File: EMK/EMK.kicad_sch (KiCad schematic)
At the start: 76 parts, among them J1 USB_C_Receptacle_USB2.0_14P, J2 Conn_01x02_Socket, J3 Conn_ARM_JTAG_SWD_10, Q1 Si2371EDS, SW1 SW_Nidec_CAS-120A1, SW10 MX9, SW11 MX13, SW12 MX10, SW13 MX14, SW14 MX11, SW15 MX15, SW16 MX12, SW17 MX16, SW2 MX1, SW3 MX2, SW4 MX3, SW5 MX4, SW6 MX5, SW7 MX6, SW8 MX7, SW9 MX8, U1 nRF52840-QFAA, U2 15nH, U3 TPS62822DLC, U4 USBLC6-2SC6, U5 TP4057, Y1 Crystal_32.768kHz, Y2 Crystal_32mHz

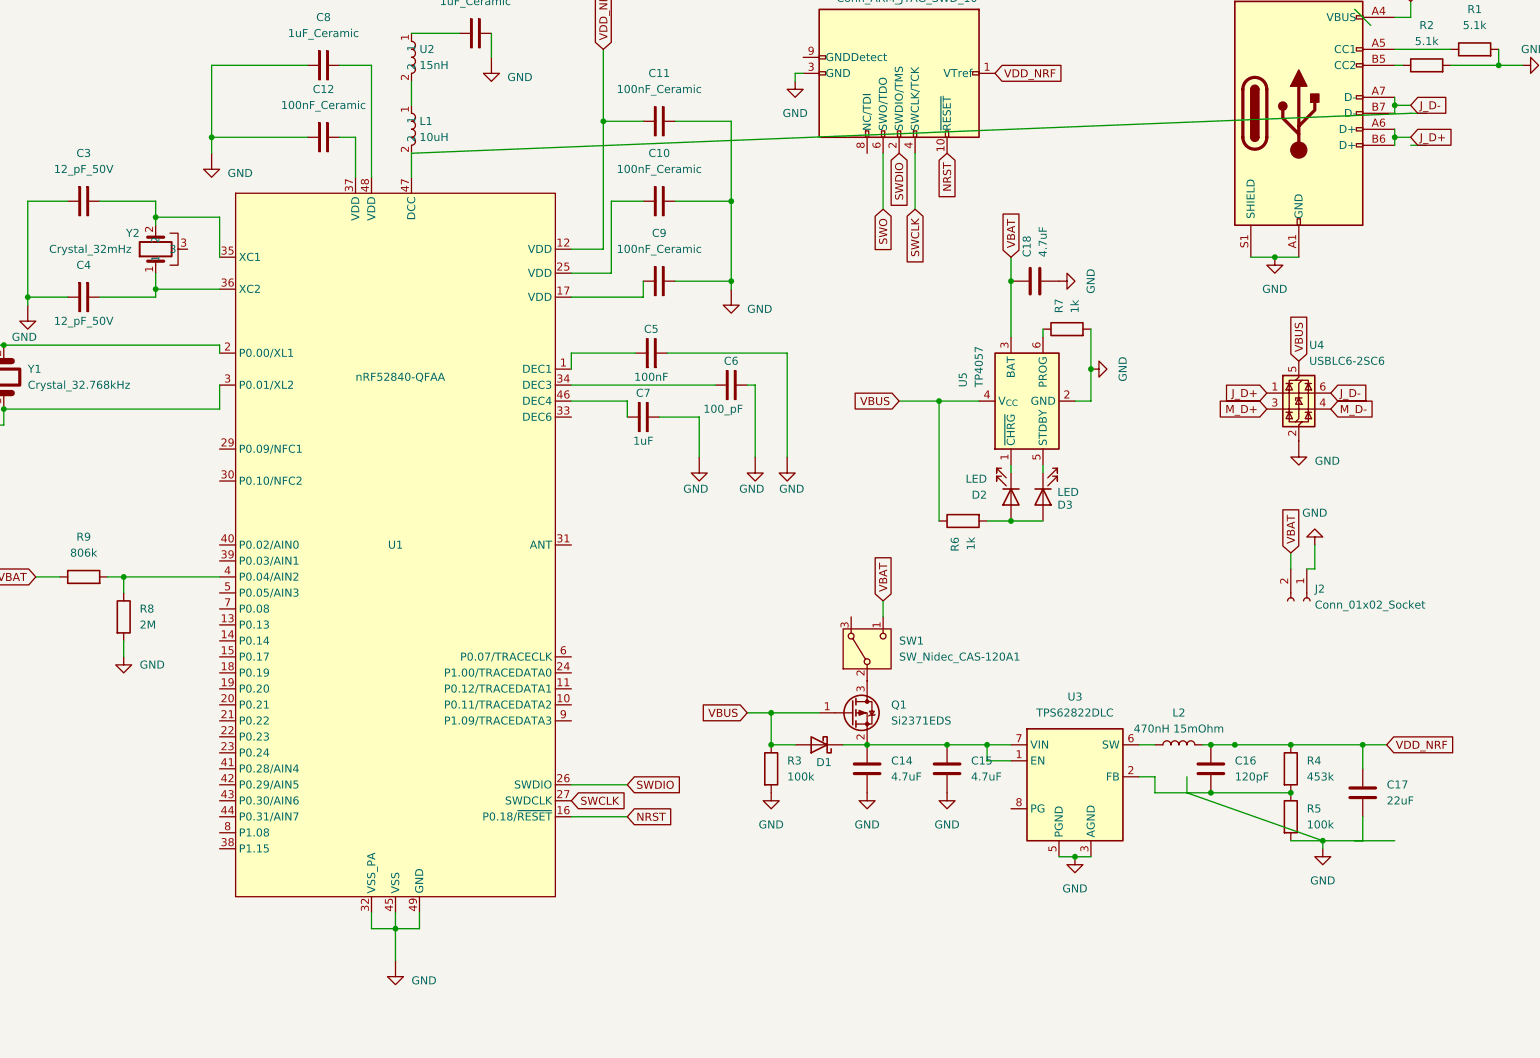
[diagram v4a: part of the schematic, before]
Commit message: feat: adiciona o conector SWD.
Signed-off-by: Paulo Santos <prms@ic.ufal.br>
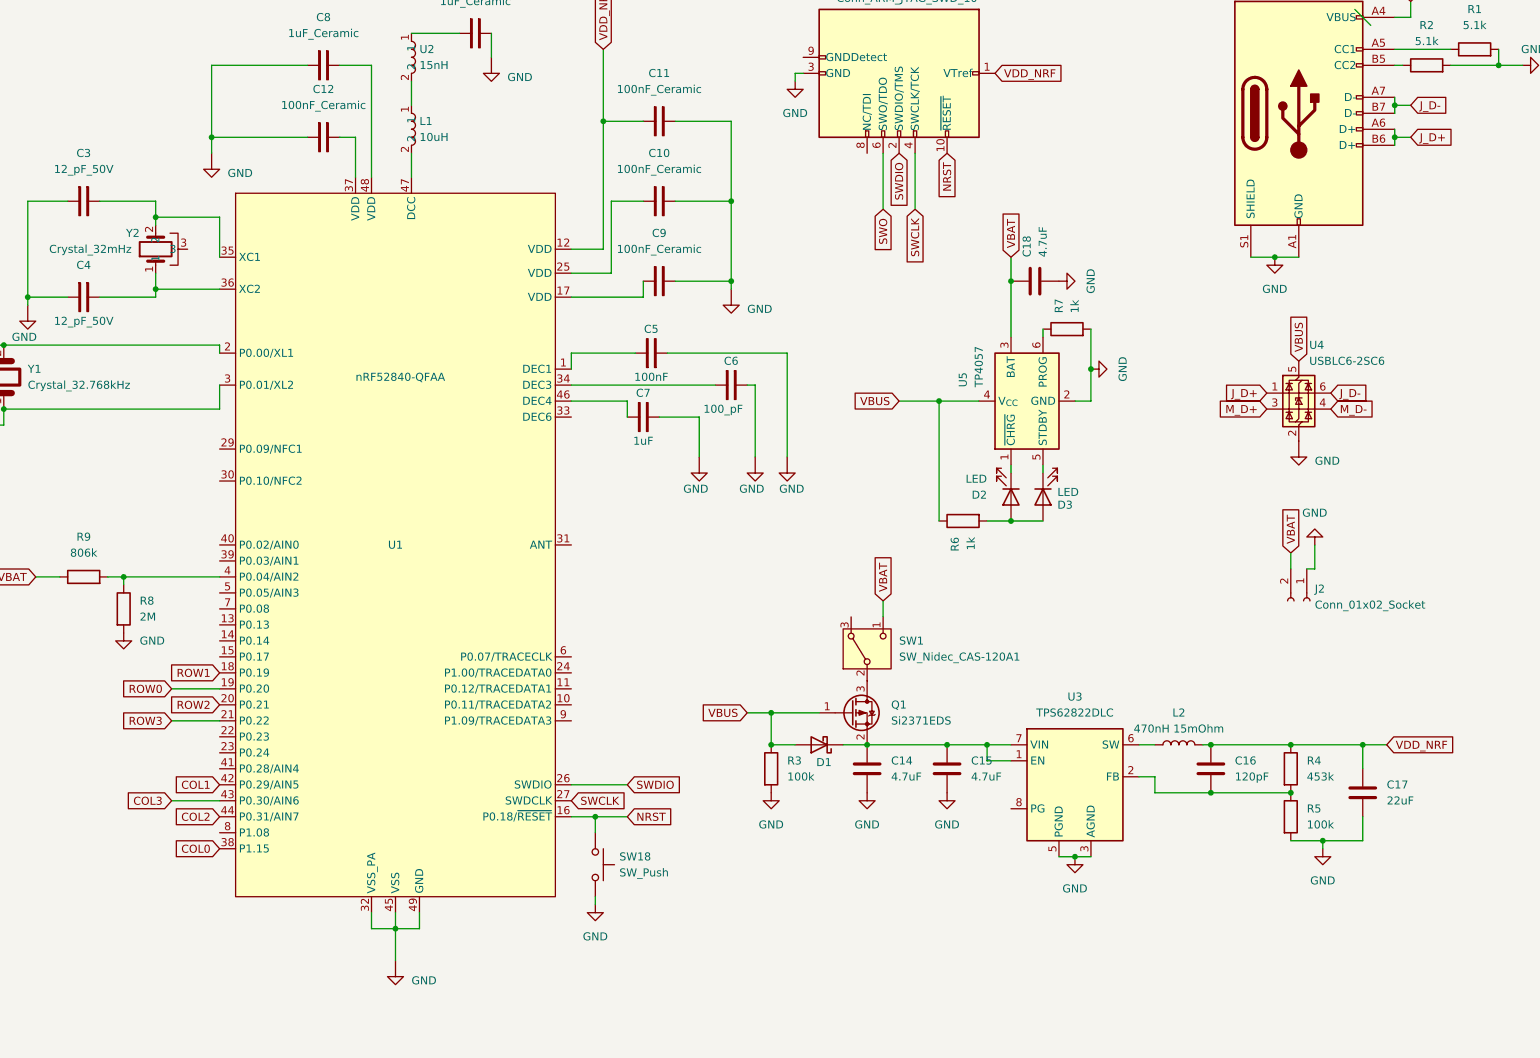
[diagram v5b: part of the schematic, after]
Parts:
- added SW18: SW_Push, symbol Switch:SW_Push
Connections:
- net COL0: now also U1.38 (P1.15)
- net COL1: now also U1.42 (P0.29/AIN5)
- net COL2: now also U1.44 (P0.31/AIN7)
- net COL3: now also U1.43 (P0.30/AIN6)
- net GND: now also SW18.2
- net NRST: now also SW18.1
- net ROW0: now also U1.19 (P0.20)
- net ROW1: now also U1.18 (P0.19)
- net ROW2: now also U1.20 (P0.21)
- net ROW3: now also U1.21 (P0.22)
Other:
- moved on the sheet: R8

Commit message: feat: organiza o esquemático e adiciona as labels aos blocos.
Signed-off-by: Paulo Santos <prms@ic.ufal.br>
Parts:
- removed D10, D11, D12, D13, D14, D15, D16, D17, D18, D19, D4, D5, D6, D7, D8, D9: D, symbol Device:D
- removed SW10: MX9, symbol Switch:SW_Push
- removed SW11: MX13, symbol Switch:SW_Push
- removed SW12: MX10, symbol Switch:SW_Push
- removed SW13: MX14, symbol Switch:SW_Push
- removed SW14: MX11, symbol Switch:SW_Push
- removed SW15: MX15, symbol Switch:SW_Push
- removed SW16: MX12, symbol Switch:SW_Push
- removed SW17: MX16, symbol Switch:SW_Push
- removed SW2: MX1, symbol Switch:SW_Push
- removed SW3: MX2, symbol Switch:SW_Push
- removed SW4: MX3, symbol Switch:SW_Push
- removed SW5: MX4, symbol Switch:SW_Push
- removed SW6: MX5, symbol Switch:SW_Push
- removed SW7: MX6, symbol Switch:SW_Push
- removed SW8: MX7, symbol Switch:SW_Push
- removed SW9: MX8, symbol Switch:SW_Push
- added C19: 1.5pF, symbol Device:C
- added C20: 1pF, symbol Device:C
- added C21: 1uF, symbol Device:C
- added L3: 3.9nH, symbol Device:L
- added R10: 0, symbol Device:R
- C10, C11, C9: value 100nF_Ceramic -> 100nF
- C6: value 100_pF -> 100pF
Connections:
- net GND: now also C19.2, C20.2
- net ANT_BT: now reaches U1.31 (ANT)
- net ANT_BT: now also C21.1, L3.2
- net VSS_PA: now reaches U1.32 (VSS_PA), U1.45 (VSS), U1.49 (GND)
- net VSS_PA: now also C21.2
- new net: C20.1, L3.1, R10.2
- new net ANT_TRACE: C19.1, R10.1
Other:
- note added: "Alimentação"
- note added: "Antena BT"
- note added: "Bateria"
- note added: "MCU"
- note added: "SWD e Debug"
- note added: "USB-C"
- title: (none) -> EMK
- moved on the sheet: C1, C10, C11, C12, C13, C14, C15, C16, C17, C18, C2, C3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

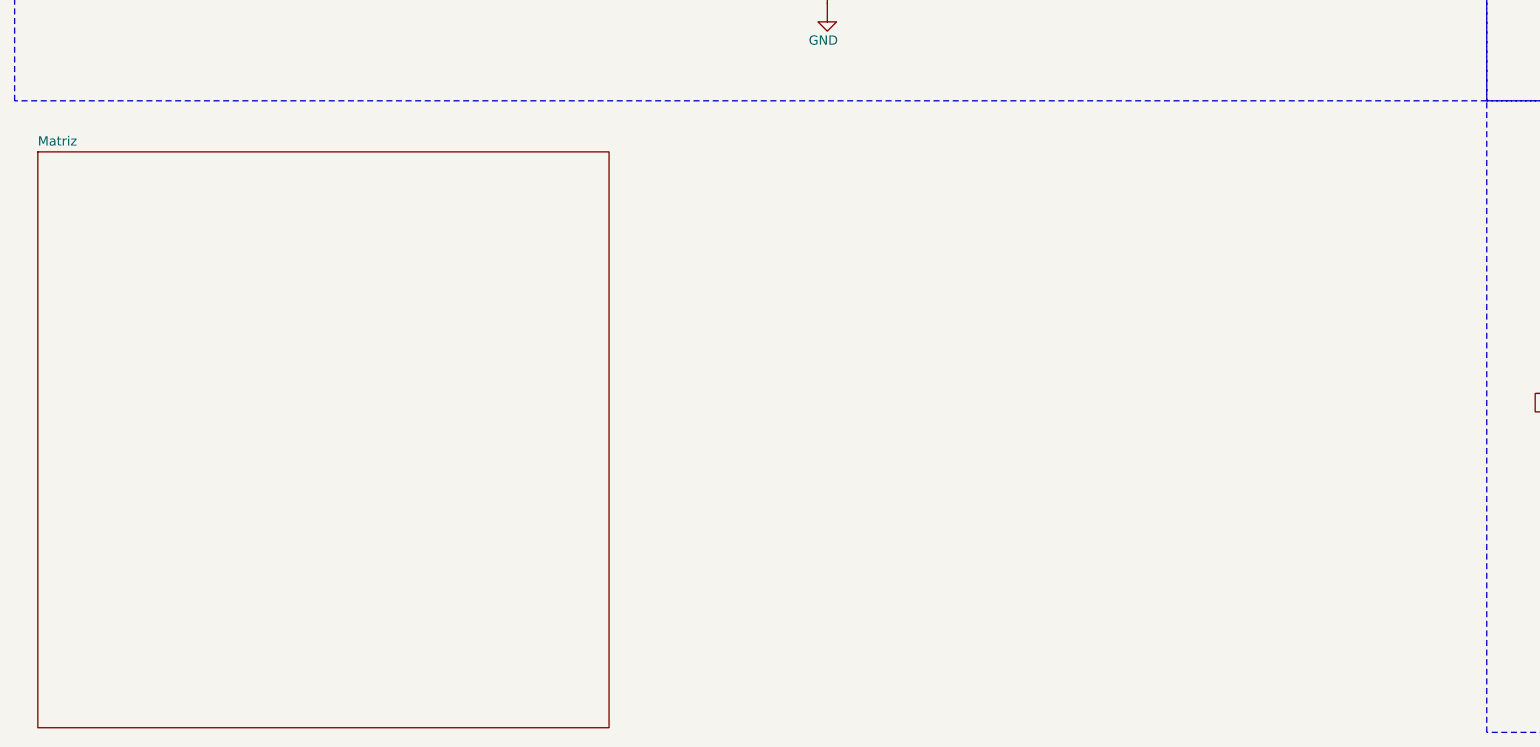
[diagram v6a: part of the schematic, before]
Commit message: feat: organiza o esquemático e adiciona as labels aos blocos.
Signed-off-by: Paulo Santos <prms@ic.ufal.br>
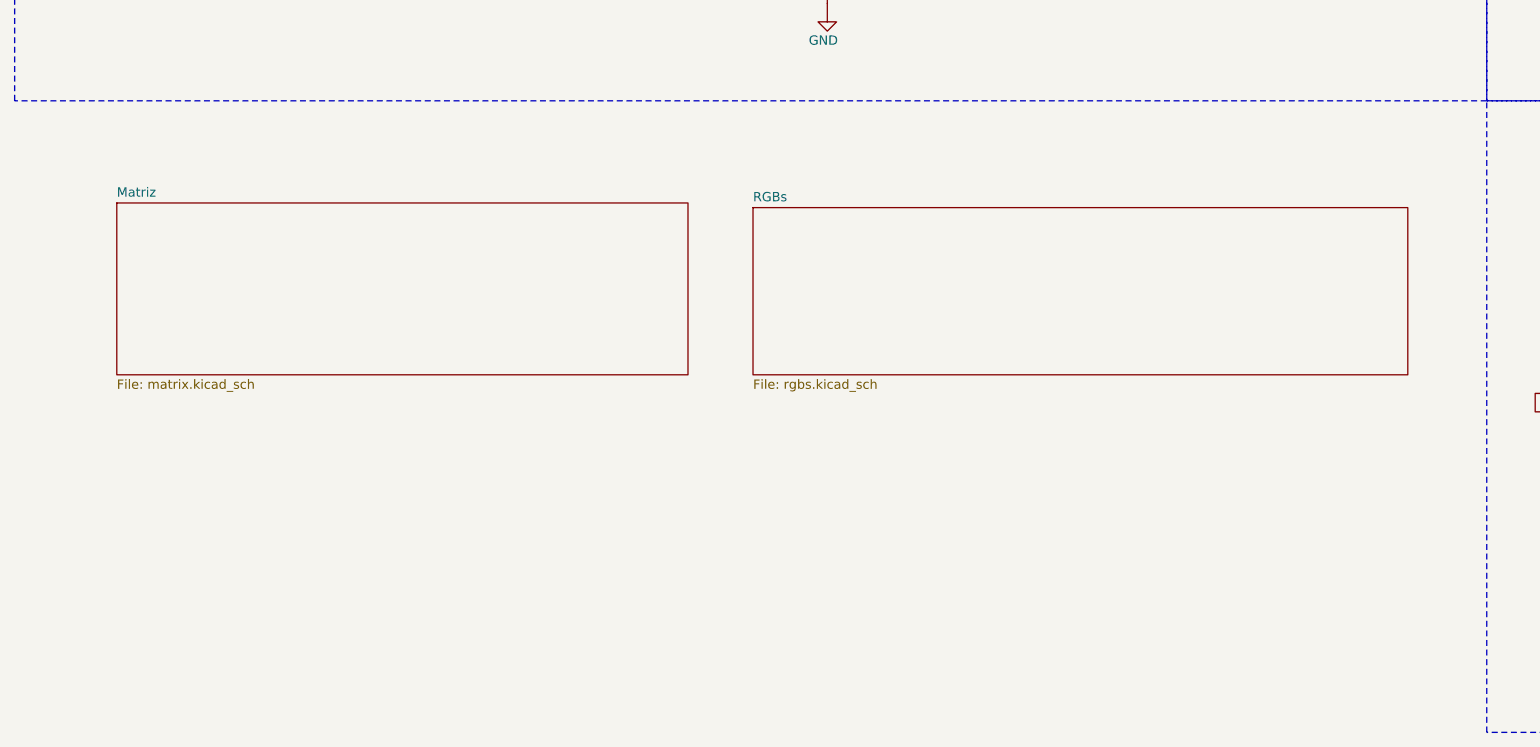
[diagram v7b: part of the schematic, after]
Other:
- added sheet RGBs (rgbs.kicad_sch)
- sheet Matriz: file untitled.kicad_sch -> matrix.kicad_sch
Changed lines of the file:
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@@
 	)
 	(sheet
-		(at 15.24 166.37)
-		(size 78.105 78.74)
+		(at 113.03 173.99)
+		(size 89.535 22.86)
+		(fields_autoplaced yes)
+		(stroke
+			(width 0.1524)
+			(type solid)
+		)
+		(fill
+			(color 0 0 0 0.0000)
+		)
+		(property "Sheetname" "RGBs"
+			(at 113.03 173.2784 0)
+			(effects
+				(font
+					(size 1.27 1.27)
+				)
+				(justify left bottom)
+			)
+		)
+		(property "Sheetfile" "rgbs.kicad_sch"
+			(at 113.03 197.4346 0)
+			(effects
+				(font
+					(size 1.27 1.27)
+				)
+				(justify left top)
+			)
+		)
+		(instances
+			(project "EMK"
+				(path "/b49e0e20-ddc2-4eb4-9509-7721d6b2744b"
+					(page "3")
+				)
+			)
+		)
+	)
+	(sheet
+		(at 26.035 173.355)
+		(size 78.105 23.495)
 		(fields_autoplaced yes)
 		(stroke
@@
 		)
 		(property "Sheetname" "Matriz"
-			(at 15.24 165.6584 0)
+			(at 26.035 172.6434 0)
 			(effects
 				(font
@@
 			)
 		)
-		(property "Sheetfile" "untitled.kicad_sch"
-			(at 15.24 245.6946 0)
+		(property "Sheetfile" "matrix.kicad_sch"
+			(at 26.035 197.4346 0)
 			(effects
 				(font
@@
 				)
 				(justify left top)
-				(hide yes)
 			)
 		)
